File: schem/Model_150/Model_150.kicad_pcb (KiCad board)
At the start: 2 copper layers, 300 x 200 mm, 321 parts, among them SW1 RESET, SW2 POWER, U0 74LS00, U1 74LS04, U10 MAX232, U11 MAX232, U12 74LS00, U13 74HCT74, U14 74LS32, U15 74LS02, U16 74LS161, U17 74LS00, U18 74AHCT125, U19 74LS04, U2 DS1233, U20 74HCT138, U21 74LS74, U22 74LS139, U23 74LS32, U24 74HCT273, U25 DS1302+, U26 74AHCT125, U27 82C55A, U28 74LS04, U29 74HCT138, U3 74AHCT125, U30 74LS08, U33 4049UB, U34 74LS76, U35 74LS76, U37 LM555xN, U38 4070, U39 74LS161, U4 74HCT139, U40 74LS00, U41 74LS161, U42 74LS74, U43 4046, U5 74HCT688, U6 74HCT273, U7 74HCT157, U8 74HCT138, U9 74HCT273

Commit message: update model 150 files to Kicad 10 (from Kicad 9)
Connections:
- D6 pad 1: Net-(D6-K) -> -12V
- D6 pad 2: -12V -> Net-(D6-A)
- D8 pad 1: Net-(D8-K) -> -5V
- D8 pad 2: -5V -> Net-(D8-A)
- R12 pad 2: Net-(D6-K) -> Net-(D6-A)
- R14 pad 2: Net-(D8-K) -> Net-(D8-A)

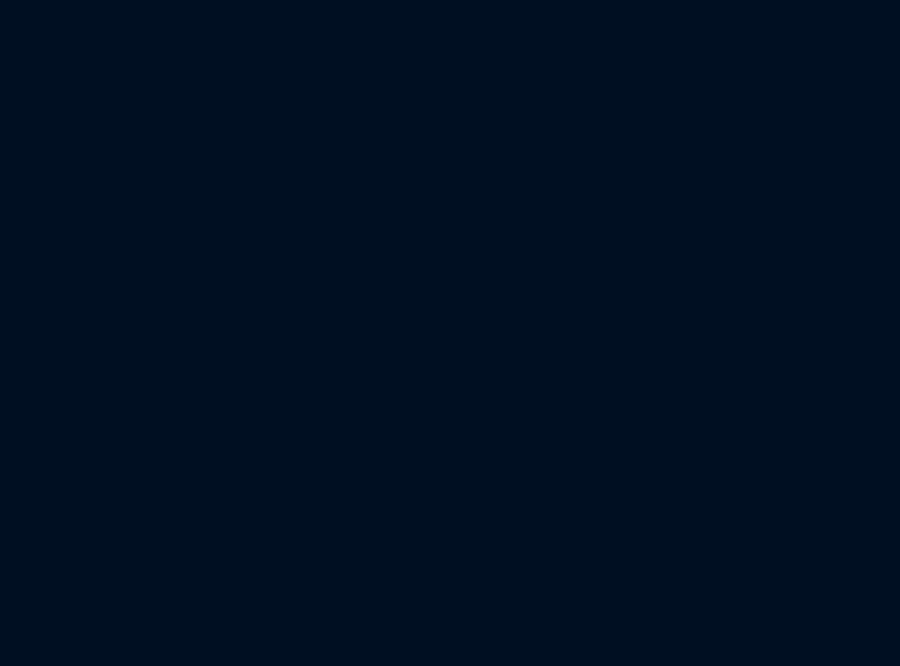
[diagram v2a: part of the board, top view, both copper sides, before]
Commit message: Assign nets, add JP5 header, add backups
Add numerous Model_150 backup ZIPs and update KiCad project files. Model_150.kicad_pcb: replace many "unconnected-..." net placeholders with proper net names (A0..A31, D0..D15, A#/D# mappings for ROM/JCBUS/IDE/FDD signals), fix a sheet path UUID, and update some testpoint/net assignments. Also add a new footprint: Connector_PinHeader_2.54mm:PinHeader_1x03 (JP5) with properties for RAM_SELECT. Project/schematic/report files were updated to reflect these changes.
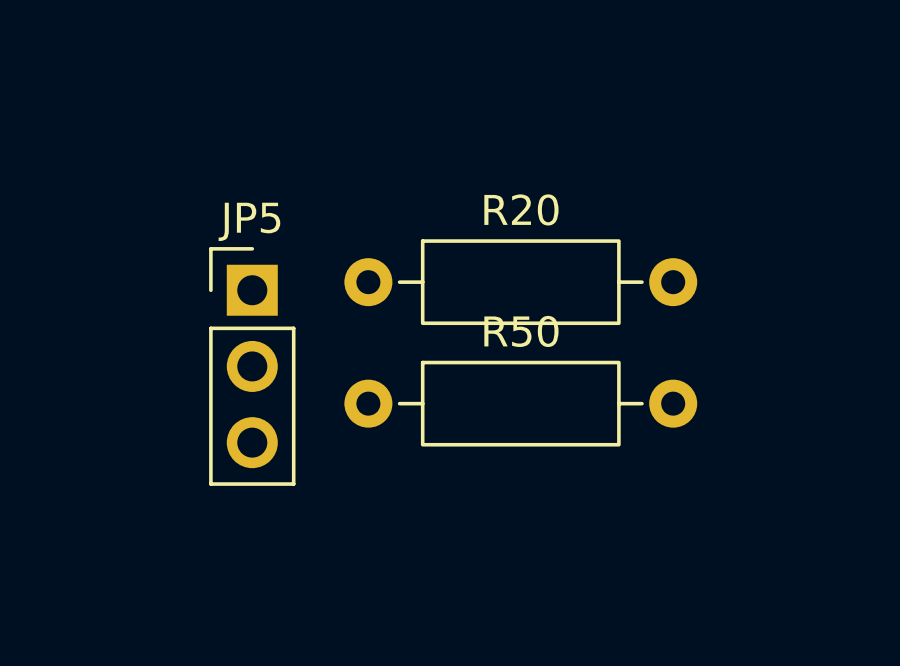
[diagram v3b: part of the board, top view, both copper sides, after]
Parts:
- added JP5: RAM_SELECT, Connector_PinHeader_2.54mm:PinHeader_1x03_P2.54mm_Vertical, F.Cu at (189.6, 45.1)
- added R20: 100K, Resistor_THT:R_Axial_DIN0207_L6.3mm_D2.5mm_P10.16mm_Horizontal, F.Cu at (193.5, 44.8)
- added R50: 100K, Resistor_THT:R_Axial_DIN0207_L6.3mm_D2.5mm_P10.16mm_Horizontal, F.Cu at (193.5, 48.9)
- R7: value R -> R?
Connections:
- net Net-(FDC_0-TC) renamed /TC
- net Net-(FDC_0-~{DACK}) renamed /DACK
- net Net-(U27-PA7) renamed /PA7
- net Net-(U4A-A0) renamed /MA19
- net Net-(U4B-A0) renamed /LA19
- net Net-(U6-Q1) renamed /LA15
- net Net-(U6-Q2) renamed /LA16
- net Net-(U6-Q3) renamed /LA17
- net Net-(U6-Q4) renamed /LA18
- CPU_0 pad 1: unconnected-(CPU_0-A11-Pad1) -> A11
- CPU_0 pad 10: unconnected-(CPU_0-D6-Pad10) -> D6
- CPU_0 pad 12: unconnected-(CPU_0-D2-Pad12) -> D2
- CPU_0 pad 13: unconnected-(CPU_0-D7-Pad13) -> D7
- CPU_0 pad 14: unconnected-(CPU_0-D0-Pad14) -> D0
- CPU_0 pad 15: unconnected-(CPU_0-D1-Pad15) -> D1
- CPU_0 pad 2: unconnected-(CPU_0-A12-Pad2) -> A12
- CPU_0 pad 3: unconnected-(CPU_0-A13-Pad3) -> A13
- CPU_0 pad 30: unconnected-(CPU_0-A0-Pad30) -> A0
- CPU_0 pad 31: unconnected-(CPU_0-A1-Pad31) -> A1
- CPU_0 pad 32: unconnected-(CPU_0-A2-Pad32) -> A2
- CPU_0 pad 33: unconnected-(CPU_0-A3-Pad33) -> A3
- CPU_0 pad 34: unconnected-(CPU_0-A4-Pad34) -> A4
- CPU_0 pad 35: unconnected-(CPU_0-A5-Pad35) -> A5
- CPU_0 pad 36: unconnected-(CPU_0-A6-Pad36) -> A6
- CPU_0 pad 37: unconnected-(CPU_0-A7-Pad37) -> A7
- CPU_0 pad 38: unconnected-(CPU_0-A8-Pad38) -> A8
- CPU_0 pad 39: unconnected-(CPU_0-A9-Pad39) -> A9
- CPU_0 pad 4: unconnected-(CPU_0-A14-Pad4) -> A14
- CPU_0 pad 40: unconnected-(CPU_0-A10-Pad40) -> A10
- CPU_0 pad 5: unconnected-(CPU_0-A15-Pad5) -> A15
- CPU_0 pad 7: unconnected-(CPU_0-D4-Pad7) -> D4
- CPU_0 pad 8: unconnected-(CPU_0-D3-Pad8) -> D3
- CPU_0 pad 9: unconnected-(CPU_0-D5-Pad9) -> D5
- CTC_0 pad 1: unconnected-(CTC_0-D4-Pad1) -> D4
- CTC_0 pad 18: unconnected-(CTC_0-CS0-Pad18) -> A0
- CTC_0 pad 19: unconnected-(CTC_0-CS1-Pad19) -> A1
- CTC_0 pad 2: unconnected-(CTC_0-D5-Pad2) -> D5
- CTC_0 pad 25: unconnected-(CTC_0-D0-Pad25) -> D0
- CTC_0 pad 26: unconnected-(CTC_0-D1-Pad26) -> D1
- CTC_0 pad 27: unconnected-(CTC_0-D2-Pad27) -> D2
- CTC_0 pad 28: unconnected-(CTC_0-D3-Pad28) -> D3
- CTC_0 pad 3: unconnected-(CTC_0-D6-Pad3) -> D6
- CTC_0 pad 4: unconnected-(CTC_0-D7-Pad4) -> D7
- DMA_0 pad 1: unconnected-(DMA_0-A5-Pad1) -> A5
- DMA_0 pad 17: unconnected-(DMA_0-A15-Pad17) -> A15
- DMA_0 pad 18: unconnected-(DMA_0-A14-Pad18) -> A14
- DMA_0 pad 19: unconnected-(DMA_0-A13-Pad19) -> A13
- DMA_0 pad 2: unconnected-(DMA_0-A4-Pad2) -> A4
- DMA_0 pad 20: unconnected-(DMA_0-A12-Pad20) -> A12
- DMA_0 pad 21: unconnected-(DMA_0-A11-Pad21) -> A11
- DMA_0 pad 22: unconnected-(DMA_0-A10-Pad22) -> A10
- DMA_0 pad 23: unconnected-(DMA_0-A9-Pad23) -> A9
- DMA_0 pad 24: unconnected-(DMA_0-A8-Pad24) -> A8
- DMA_0 pad 27: unconnected-(DMA_0-D7-Pad27) -> D7
- DMA_0 pad 28: unconnected-(DMA_0-D6-Pad28) -> D6
- DMA_0 pad 29: unconnected-(DMA_0-D5-Pad29) -> D5
- DMA_0 pad 3: unconnected-(DMA_0-A3-Pad3) -> A3
- DMA_0 pad 31: unconnected-(DMA_0-D4-Pad31) -> D4
- DMA_0 pad 32: unconnected-(DMA_0-D3-Pad32) -> D3
- DMA_0 pad 33: unconnected-(DMA_0-D2-Pad33) -> D2
- DMA_0 pad 34: unconnected-(DMA_0-D1-Pad34) -> D1
- DMA_0 pad 35: unconnected-(DMA_0-D0-Pad35) -> D0
- DMA_0 pad 39: unconnected-(DMA_0-A7-Pad39) -> A7
- DMA_0 pad 4: unconnected-(DMA_0-A2-Pad4) -> A2
- DMA_0 pad 40: unconnected-(DMA_0-A6-Pad40) -> A6
- DMA_0 pad 5: unconnected-(DMA_0-A1-Pad5) -> A1
- DMA_0 pad 6: unconnected-(DMA_0-A0-Pad6) -> A0
- FDC_0 pad 10: unconnected-(FDC_0-DB3-Pad10) -> D3
- FDC_0 pad 11: unconnected-(FDC_0-DB4-Pad11) -> D4
- FDC_0 pad 12: unconnected-(FDC_0-DB5-Pad12) -> D5
- FDC_0 pad 13: unconnected-(FDC_0-DB6-Pad13) -> D6
- FDC_0 pad 14: unconnected-(FDC_0-DB7-Pad14) -> D7
- FDC_0 pad 4: ADDRESS -> A[0..31]
- FDC_0 pad 7: unconnected-(FDC_0-DB0-Pad7) -> D0
- FDC_0 pad 8: unconnected-(FDC_0-DB1-Pad8) -> D1
- FDC_0 pad 9: unconnected-(FDC_0-DB2-Pad9) -> D2
- FDD_0 pad 34: Net-(FDC_0-WP) -> Net-(FDD_0-Pin_34)
- FPU_0 pad 10: unconnected-(FPU_0-DB2-Pad10) -> D2
- FPU_0 pad 11: unconnected-(FPU_0-DB3-Pad11) -> D3
- FPU_0 pad 12: unconnected-(FPU_0-DB4-Pad12) -> D4
- FPU_0 pad 13: unconnected-(FPU_0-DB5-Pad13) -> D5
- FPU_0 pad 14: unconnected-(FPU_0-DB6-Pad14) -> D6
- FPU_0 pad 15: unconnected-(FPU_0-DB7-Pad15) -> D7
- FPU_0 pad 21: ADDRESS -> A[0..31]
- FPU_0 pad 8: unconnected-(FPU_0-DB0-Pad8) -> D0
- FPU_0 pad 9: unconnected-(FPU_0-DB1-Pad9) -> D1
- IDE_1 pad 33: unconnected-(IDE_1-Pin_33-Pad33) -> A1
- IDE_1 pad 35: unconnected-(IDE_1-Pin_35-Pad35) -> A0
- IDE_1 pad 36: unconnected-(IDE_1-Pin_36-Pad36) -> A2
- JCBUS_0 pad a10: unconnected-(JCBUS_0-Pin_a10-Pada10) -> A1
- JCBUS_0 pad a11: unconnected-(JCBUS_0-Pin_a11-Pada11) -> A2
- JCBUS_0 pad a12: unconnected-(JCBUS_0-Pin_a12-Pada12) -> A3
- JCBUS_0 pad a13: unconnected-(JCBUS_0-Pin_a13-Pada13) -> A4
- JCBUS_0 pad a14: unconnected-(JCBUS_0-Pin_a14-Pada14) -> A5
- JCBUS_0 pad a15: unconnected-(JCBUS_0-Pin_a15-Pada15) -> A6
- JCBUS_0 pad a16: unconnected-(JCBUS_0-Pin_a16-Pada16) -> A7
- JCBUS_0 pad a17: unconnected-(JCBUS_0-Pin_a17-Pada17) -> A8
- JCBUS_0 pad a18: unconnected-(JCBUS_0-Pin_a18-Pada18) -> A9
- JCBUS_0 pad a19: unconnected-(JCBUS_0-Pin_a19-Pada19) -> A10
- JCBUS_0 pad a20: unconnected-(JCBUS_0-Pin_a20-Pada20) -> A11
- JCBUS_0 pad a21: unconnected-(JCBUS_0-Pin_a21-Pada21) -> A12
- JCBUS_0 pad a22: unconnected-(JCBUS_0-Pin_a22-Pada22) -> A13
- JCBUS_0 pad a23: unconnected-(JCBUS_0-Pin_a23-Pada23) -> A14
- JCBUS_0 pad a24: unconnected-(JCBUS_0-Pin_a24-Pada24) -> A15
- JCBUS_0 pad a25: unconnected-(JCBUS_0-Pin_a25-Pada25) -> A16
- JCBUS_0 pad a26: unconnected-(JCBUS_0-Pin_a26-Pada26) -> A17
- JCBUS_0 pad a27: unconnected-(JCBUS_0-Pin_a27-Pada27) -> A18
- JCBUS_0 pad a28: unconnected-(JCBUS_0-Pin_a28-Pada28) -> A19
- JCBUS_0 pad a29: unconnected-(JCBUS_0-Pin_a29-Pada29) -> A20
- JCBUS_0 pad a30: unconnected-(JCBUS_0-Pin_a30-Pada30) -> A21
- JCBUS_0 pad a31: unconnected-(JCBUS_0-Pin_a31-Pada31) -> A22
- JCBUS_0 pad a32: unconnected-(JCBUS_0-Pin_a32-Pada32) -> A23
- JCBUS_0 pad a33: unconnected-(JCBUS_0-Pin_a33-Pada33) -> A24
- JCBUS_0 pad a34: unconnected-(JCBUS_0-Pin_a34-Pada34) -> A25
- JCBUS_0 pad a35: unconnected-(JCBUS_0-Pin_a35-Pada35) -> A26
- JCBUS_0 pad a36: unconnected-(JCBUS_0-Pin_a36-Pada36) -> A27
- JCBUS_0 pad a37: unconnected-(JCBUS_0-Pin_a37-Pada37) -> A28
- JCBUS_0 pad a38: unconnected-(JCBUS_0-Pin_a38-Pada38) -> A29
- JCBUS_0 pad a39: unconnected-(JCBUS_0-Pin_a39-Pada39) -> A30
- JCBUS_0 pad a40: unconnected-(JCBUS_0-Pin_a40-Pada40) -> A31
- JCBUS_0 pad a9: unconnected-(JCBUS_0-Pin_a9-Pada9) -> A0
- JCBUS_0 pad b25: unconnected-(JCBUS_0-Pin_b25-Padb25) -> D0
- JCBUS_0 pad b26: unconnected-(JCBUS_0-Pin_b26-Padb26) -> D1
- JCBUS_0 pad b27: unconnected-(JCBUS_0-Pin_b27-Padb27) -> D2
- JCBUS_0 pad b28: unconnected-(JCBUS_0-Pin_b28-Padb28) -> D3
- JCBUS_0 pad b29: unconnected-(JCBUS_0-Pin_b29-Padb29) -> D4
- JCBUS_0 pad b30: unconnected-(JCBUS_0-Pin_b30-Padb30) -> D5
- JCBUS_0 pad b31: unconnected-(JCBUS_0-Pin_b31-Padb31) -> D6
- JCBUS_0 pad b32: unconnected-(JCBUS_0-Pin_b32-Padb32) -> D7
- JCBUS_0 pad b33: unconnected-(JCBUS_0-Pin_b33-Padb33) -> D8
- JCBUS_0 pad b34: unconnected-(JCBUS_0-Pin_b34-Padb34) -> D9
- JCBUS_0 pad b35: unconnected-(JCBUS_0-Pin_b35-Padb35) -> D10
- JCBUS_0 pad b36: unconnected-(JCBUS_0-Pin_b36-Padb36) -> D11
- JCBUS_0 pad b37: unconnected-(JCBUS_0-Pin_b37-Padb37) -> D12
- JCBUS_0 pad b38: unconnected-(JCBUS_0-Pin_b38-Padb38) -> D13
- JCBUS_0 pad b39: unconnected-(JCBUS_0-Pin_b39-Padb39) -> D14
- JCBUS_0 pad b40: unconnected-(JCBUS_0-Pin_b40-Padb40) -> D15
- JCBUS_1 pad a10: unconnected-(JCBUS_1-Pin_a10-Pada10) -> A1
- JCBUS_1 pad a11: unconnected-(JCBUS_1-Pin_a11-Pada11) -> A2
- JCBUS_1 pad a12: unconnected-(JCBUS_1-Pin_a12-Pada12) -> A3
- JCBUS_1 pad a13: unconnected-(JCBUS_1-Pin_a13-Pada13) -> A4
- JCBUS_1 pad a14: unconnected-(JCBUS_1-Pin_a14-Pada14) -> A5
- JCBUS_1 pad a15: unconnected-(JCBUS_1-Pin_a15-Pada15) -> A6
- JCBUS_1 pad a16: unconnected-(JCBUS_1-Pin_a16-Pada16) -> A7
- JCBUS_1 pad a17: unconnected-(JCBUS_1-Pin_a17-Pada17) -> A8
- JCBUS_1 pad a18: unconnected-(JCBUS_1-Pin_a18-Pada18) -> A9
- JCBUS_1 pad a19: unconnected-(JCBUS_1-Pin_a19-Pada19) -> A10
- JCBUS_1 pad a20: unconnected-(JCBUS_1-Pin_a20-Pada20) -> A11
- JCBUS_1 pad a21: unconnected-(JCBUS_1-Pin_a21-Pada21) -> A12
- JCBUS_1 pad a22: unconnected-(JCBUS_1-Pin_a22-Pada22) -> A13
- JCBUS_1 pad a23: unconnected-(JCBUS_1-Pin_a23-Pada23) -> A14
- JCBUS_1 pad a24: unconnected-(JCBUS_1-Pin_a24-Pada24) -> A15
- JCBUS_1 pad a25: unconnected-(JCBUS_1-Pin_a25-Pada25) -> A16
- JCBUS_1 pad a26: unconnected-(JCBUS_1-Pin_a26-Pada26) -> A17
- JCBUS_1 pad a27: unconnected-(JCBUS_1-Pin_a27-Pada27) -> A18
- JCBUS_1 pad a28: unconnected-(JCBUS_1-Pin_a28-Pada28) -> A19
- JCBUS_1 pad a29: unconnected-(JCBUS_1-Pin_a29-Pada29) -> A20
- JCBUS_1 pad a30: unconnected-(JCBUS_1-Pin_a30-Pada30) -> A21
- JCBUS_1 pad a31: unconnected-(JCBUS_1-Pin_a31-Pada31) -> A22
- JCBUS_1 pad a32: unconnected-(JCBUS_1-Pin_a32-Pada32) -> A23
- JCBUS_1 pad a33: unconnected-(JCBUS_1-Pin_a33-Pada33) -> A24
- JCBUS_1 pad a34: unconnected-(JCBUS_1-Pin_a34-Pada34) -> A25
- JCBUS_1 pad a35: unconnected-(JCBUS_1-Pin_a35-Pada35) -> A26
- JCBUS_1 pad a36: unconnected-(JCBUS_1-Pin_a36-Pada36) -> A27
- JCBUS_1 pad a37: unconnected-(JCBUS_1-Pin_a37-Pada37) -> A28
- JCBUS_1 pad a38: unconnected-(JCBUS_1-Pin_a38-Pada38) -> A29
- JCBUS_1 pad a39: unconnected-(JCBUS_1-Pin_a39-Pada39) -> A30
- JCBUS_1 pad a40: unconnected-(JCBUS_1-Pin_a40-Pada40) -> A31
- JCBUS_1 pad a9: unconnected-(JCBUS_1-Pin_a9-Pada9) -> A0
- JCBUS_1 pad b25: unconnected-(JCBUS_1-Pin_b25-Padb25) -> D0
- JCBUS_1 pad b26: unconnected-(JCBUS_1-Pin_b26-Padb26) -> D1
- JCBUS_1 pad b27: unconnected-(JCBUS_1-Pin_b27-Padb27) -> D2
- JCBUS_1 pad b28: unconnected-(JCBUS_1-Pin_b28-Padb28) -> D3
- JCBUS_1 pad b29: unconnected-(JCBUS_1-Pin_b29-Padb29) -> D4
- JCBUS_1 pad b30: unconnected-(JCBUS_1-Pin_b30-Padb30) -> D5
- JCBUS_1 pad b31: unconnected-(JCBUS_1-Pin_b31-Padb31) -> D6
- JCBUS_1 pad b32: unconnected-(JCBUS_1-Pin_b32-Padb32) -> D7
- JCBUS_1 pad b33: unconnected-(JCBUS_1-Pin_b33-Padb33) -> D8
- JCBUS_1 pad b34: unconnected-(JCBUS_1-Pin_b34-Padb34) -> D9
- JCBUS_1 pad b35: unconnected-(JCBUS_1-Pin_b35-Padb35) -> D10
- JCBUS_1 pad b36: unconnected-(JCBUS_1-Pin_b36-Padb36) -> D11
- JCBUS_1 pad b37: unconnected-(JCBUS_1-Pin_b37-Padb37) -> D12
- JCBUS_1 pad b38: unconnected-(JCBUS_1-Pin_b38-Padb38) -> D13
- JCBUS_1 pad b39: unconnected-(JCBUS_1-Pin_b39-Padb39) -> D14
- JCBUS_1 pad b40: unconnected-(JCBUS_1-Pin_b40-Padb40) -> D15
- JCBUS_2 pad a10: unconnected-(JCBUS_2-Pin_a10-Pada10) -> A1
- JCBUS_2 pad a11: unconnected-(JCBUS_2-Pin_a11-Pada11) -> A2
- JCBUS_2 pad a12: unconnected-(JCBUS_2-Pin_a12-Pada12) -> A3
- JCBUS_2 pad a13: unconnected-(JCBUS_2-Pin_a13-Pada13) -> A4
- JCBUS_2 pad a14: unconnected-(JCBUS_2-Pin_a14-Pada14) -> A5
- JCBUS_2 pad a15: unconnected-(JCBUS_2-Pin_a15-Pada15) -> A6
- JCBUS_2 pad a16: unconnected-(JCBUS_2-Pin_a16-Pada16) -> A7
- JCBUS_2 pad a17: unconnected-(JCBUS_2-Pin_a17-Pada17) -> A8
- JCBUS_2 pad a18: unconnected-(JCBUS_2-Pin_a18-Pada18) -> A9
- JCBUS_2 pad a19: unconnected-(JCBUS_2-Pin_a19-Pada19) -> A10
- JCBUS_2 pad a20: unconnected-(JCBUS_2-Pin_a20-Pada20) -> A11
- JCBUS_2 pad a21: unconnected-(JCBUS_2-Pin_a21-Pada21) -> A12
- JCBUS_2 pad a22: unconnected-(JCBUS_2-Pin_a22-Pada22) -> A13
- JCBUS_2 pad a23: unconnected-(JCBUS_2-Pin_a23-Pada23) -> A14
- JCBUS_2 pad a24: unconnected-(JCBUS_2-Pin_a24-Pada24) -> A15
- JCBUS_2 pad a25: unconnected-(JCBUS_2-Pin_a25-Pada25) -> A16
- JCBUS_2 pad a26: unconnected-(JCBUS_2-Pin_a26-Pada26) -> A17
- JCBUS_2 pad a27: unconnected-(JCBUS_2-Pin_a27-Pada27) -> A18
- JCBUS_2 pad a28: unconnected-(JCBUS_2-Pin_a28-Pada28) -> A19
- JCBUS_2 pad a29: unconnected-(JCBUS_2-Pin_a29-Pada29) -> A20
- JCBUS_2 pad a30: unconnected-(JCBUS_2-Pin_a30-Pada30) -> A21
- JCBUS_2 pad a31: unconnected-(JCBUS_2-Pin_a31-Pada31) -> A22
- JCBUS_2 pad a32: unconnected-(JCBUS_2-Pin_a32-Pada32) -> A23
- JCBUS_2 pad a33: unconnected-(JCBUS_2-Pin_a33-Pada33) -> A24
- JCBUS_2 pad a34: unconnected-(JCBUS_2-Pin_a34-Pada34) -> A25
- JCBUS_2 pad a35: unconnected-(JCBUS_2-Pin_a35-Pada35) -> A26
- JCBUS_2 pad a36: unconnected-(JCBUS_2-Pin_a36-Pada36) -> A27
- JCBUS_2 pad a37: unconnected-(JCBUS_2-Pin_a37-Pada37) -> A28
- JCBUS_2 pad a38: unconnected-(JCBUS_2-Pin_a38-Pada38) -> A29
- JCBUS_2 pad a39: unconnected-(JCBUS_2-Pin_a39-Pada39) -> A30
- JCBUS_2 pad a40: unconnected-(JCBUS_2-Pin_a40-Pada40) -> A31
- JCBUS_2 pad a9: unconnected-(JCBUS_2-Pin_a9-Pada9) -> A0
- JCBUS_2 pad b25: unconnected-(JCBUS_2-Pin_b25-Padb25) -> D0
- JCBUS_2 pad b26: unconnected-(JCBUS_2-Pin_b26-Padb26) -> D1
- JCBUS_2 pad b27: unconnected-(JCBUS_2-Pin_b27-Padb27) -> D2
- JCBUS_2 pad b28: unconnected-(JCBUS_2-Pin_b28-Padb28) -> D3
- JCBUS_2 pad b29: unconnected-(JCBUS_2-Pin_b29-Padb29) -> D4
- JCBUS_2 pad b30: unconnected-(JCBUS_2-Pin_b30-Padb30) -> D5
- JCBUS_2 pad b31: unconnected-(JCBUS_2-Pin_b31-Padb31) -> D6
- JCBUS_2 pad b32: unconnected-(JCBUS_2-Pin_b32-Padb32) -> D7
- JCBUS_2 pad b33: unconnected-(JCBUS_2-Pin_b33-Padb33) -> D8
- JCBUS_2 pad b34: unconnected-(JCBUS_2-Pin_b34-Padb34) -> D9
- JCBUS_2 pad b35: unconnected-(JCBUS_2-Pin_b35-Padb35) -> D10
- JCBUS_2 pad b36: unconnected-(JCBUS_2-Pin_b36-Padb36) -> D11
- JCBUS_2 pad b37: unconnected-(JCBUS_2-Pin_b37-Padb37) -> D12
- JCBUS_2 pad b38: unconnected-(JCBUS_2-Pin_b38-Padb38) -> D13
- JCBUS_2 pad b39: unconnected-(JCBUS_2-Pin_b39-Padb39) -> D14
- JCBUS_2 pad b40: unconnected-(JCBUS_2-Pin_b40-Padb40) -> D15
- JCBUS_3 pad a10: unconnected-(JCBUS_3-Pin_a10-Pada10) -> A1
- JCBUS_3 pad a11: unconnected-(JCBUS_3-Pin_a11-Pada11) -> A2
- JCBUS_3 pad a12: unconnected-(JCBUS_3-Pin_a12-Pada12) -> A3
- JCBUS_3 pad a13: unconnected-(JCBUS_3-Pin_a13-Pada13) -> A4
- JCBUS_3 pad a14: unconnected-(JCBUS_3-Pin_a14-Pada14) -> A5
- JCBUS_3 pad a15: unconnected-(JCBUS_3-Pin_a15-Pada15) -> A6
- JCBUS_3 pad a16: unconnected-(JCBUS_3-Pin_a16-Pada16) -> A7
- JCBUS_3 pad a17: unconnected-(JCBUS_3-Pin_a17-Pada17) -> A8
- JCBUS_3 pad a18: unconnected-(JCBUS_3-Pin_a18-Pada18) -> A9
- JCBUS_3 pad a19: unconnected-(JCBUS_3-Pin_a19-Pada19) -> A10
- JCBUS_3 pad a20: unconnected-(JCBUS_3-Pin_a20-Pada20) -> A11
- JCBUS_3 pad a21: unconnected-(JCBUS_3-Pin_a21-Pada21) -> A12
- JCBUS_3 pad a22: unconnected-(JCBUS_3-Pin_a22-Pada22) -> A13
- JCBUS_3 pad a23: unconnected-(JCBUS_3-Pin_a23-Pada23) -> A14
- JCBUS_3 pad a24: unconnected-(JCBUS_3-Pin_a24-Pada24) -> A15
- JCBUS_3 pad a25: unconnected-(JCBUS_3-Pin_a25-Pada25) -> A16
- JCBUS_3 pad a26: unconnected-(JCBUS_3-Pin_a26-Pada26) -> A17
- JCBUS_3 pad a27: unconnected-(JCBUS_3-Pin_a27-Pada27) -> A18
- JCBUS_3 pad a28: unconnected-(JCBUS_3-Pin_a28-Pada28) -> A19
- JCBUS_3 pad a29: unconnected-(JCBUS_3-Pin_a29-Pada29) -> A20
- JCBUS_3 pad a30: unconnected-(JCBUS_3-Pin_a30-Pada30) -> A21
- JCBUS_3 pad a31: unconnected-(JCBUS_3-Pin_a31-Pada31) -> A22
- JCBUS_3 pad a32: unconnected-(JCBUS_3-Pin_a32-Pada32) -> A23
- JCBUS_3 pad a33: unconnected-(JCBUS_3-Pin_a33-Pada33) -> A24
- JCBUS_3 pad a34: unconnected-(JCBUS_3-Pin_a34-Pada34) -> A25
- JCBUS_3 pad a35: unconnected-(JCBUS_3-Pin_a35-Pada35) -> A26
- JCBUS_3 pad a36: unconnected-(JCBUS_3-Pin_a36-Pada36) -> A27
- JCBUS_3 pad a37: unconnected-(JCBUS_3-Pin_a37-Pada37) -> A28
- JCBUS_3 pad a38: unconnected-(JCBUS_3-Pin_a38-Pada38) -> A29
- JCBUS_3 pad a39: unconnected-(JCBUS_3-Pin_a39-Pada39) -> A30
- JCBUS_3 pad a40: unconnected-(JCBUS_3-Pin_a40-Pada40) -> A31
- JCBUS_3 pad a9: unconnected-(JCBUS_3-Pin_a9-Pada9) -> A0
- JCBUS_3 pad b25: unconnected-(JCBUS_3-Pin_b25-Padb25) -> D0
- JCBUS_3 pad b26: unconnected-(JCBUS_3-Pin_b26-Padb26) -> D1
- JCBUS_3 pad b27: unconnected-(JCBUS_3-Pin_b27-Padb27) -> D2
- JCBUS_3 pad b28: unconnected-(JCBUS_3-Pin_b28-Padb28) -> D3
- JCBUS_3 pad b29: unconnected-(JCBUS_3-Pin_b29-Padb29) -> D4
- JCBUS_3 pad b30: unconnected-(JCBUS_3-Pin_b30-Padb30) -> D5
- JCBUS_3 pad b31: unconnected-(JCBUS_3-Pin_b31-Padb31) -> D6
- JCBUS_3 pad b32: unconnected-(JCBUS_3-Pin_b32-Padb32) -> D7
- JCBUS_3 pad b33: unconnected-(JCBUS_3-Pin_b33-Padb33) -> D8
- JCBUS_3 pad b34: unconnected-(JCBUS_3-Pin_b34-Padb34) -> D9
- JCBUS_3 pad b35: unconnected-(JCBUS_3-Pin_b35-Padb35) -> D10
- JCBUS_3 pad b36: unconnected-(JCBUS_3-Pin_b36-Padb36) -> D11
- JCBUS_3 pad b37: unconnected-(JCBUS_3-Pin_b37-Padb37) -> D12
- JCBUS_3 pad b38: unconnected-(JCBUS_3-Pin_b38-Padb38) -> D13
- JCBUS_3 pad b39: unconnected-(JCBUS_3-Pin_b39-Padb39) -> D14
- JCBUS_3 pad b40: unconnected-(JCBUS_3-Pin_b40-Padb40) -> D15
- JCBUS_4 pad a10: unconnected-(JCBUS_4-Pin_a10-Pada10) -> A1
- JCBUS_4 pad a11: unconnected-(JCBUS_4-Pin_a11-Pada11) -> A2
- JCBUS_4 pad a12: unconnected-(JCBUS_4-Pin_a12-Pada12) -> A3
- JCBUS_4 pad a13: unconnected-(JCBUS_4-Pin_a13-Pada13) -> A4
- JCBUS_4 pad a14: unconnected-(JCBUS_4-Pin_a14-Pada14) -> A5
- JCBUS_4 pad a15: unconnected-(JCBUS_4-Pin_a15-Pada15) -> A6
- JCBUS_4 pad a16: unconnected-(JCBUS_4-Pin_a16-Pada16) -> A7
- JCBUS_4 pad a17: unconnected-(JCBUS_4-Pin_a17-Pada17) -> A8
- JCBUS_4 pad a18: unconnected-(JCBUS_4-Pin_a18-Pada18) -> A9
- JCBUS_4 pad a19: unconnected-(JCBUS_4-Pin_a19-Pada19) -> A10
- JCBUS_4 pad a20: unconnected-(JCBUS_4-Pin_a20-Pada20) -> A11
- JCBUS_4 pad a21: unconnected-(JCBUS_4-Pin_a21-Pada21) -> A12
- JCBUS_4 pad a22: unconnected-(JCBUS_4-Pin_a22-Pada22) -> A13
- JCBUS_4 pad a23: unconnected-(JCBUS_4-Pin_a23-Pada23) -> A14
- JCBUS_4 pad a24: unconnected-(JCBUS_4-Pin_a24-Pada24) -> A15
- JCBUS_4 pad a25: unconnected-(JCBUS_4-Pin_a25-Pada25) -> A16
- JCBUS_4 pad a26: unconnected-(JCBUS_4-Pin_a26-Pada26) -> A17
- JCBUS_4 pad a27: unconnected-(JCBUS_4-Pin_a27-Pada27) -> A18
- JCBUS_4 pad a28: unconnected-(JCBUS_4-Pin_a28-Pada28) -> A19
- JCBUS_4 pad a29: unconnected-(JCBUS_4-Pin_a29-Pada29) -> A20
- JCBUS_4 pad a30: unconnected-(JCBUS_4-Pin_a30-Pada30) -> A21
- JCBUS_4 pad a31: unconnected-(JCBUS_4-Pin_a31-Pada31) -> A22
- JCBUS_4 pad a32: unconnected-(JCBUS_4-Pin_a32-Pada32) -> A23
- JCBUS_4 pad a33: unconnected-(JCBUS_4-Pin_a33-Pada33) -> A24
- JCBUS_4 pad a34: unconnected-(JCBUS_4-Pin_a34-Pada34) -> A25
- JCBUS_4 pad a35: unconnected-(JCBUS_4-Pin_a35-Pada35) -> A26
- JCBUS_4 pad a36: unconnected-(JCBUS_4-Pin_a36-Pada36) -> A27
- JCBUS_4 pad a37: unconnected-(JCBUS_4-Pin_a37-Pada37) -> A28
- JCBUS_4 pad a38: unconnected-(JCBUS_4-Pin_a38-Pada38) -> A29
- JCBUS_4 pad a39: unconnected-(JCBUS_4-Pin_a39-Pada39) -> A30
- JCBUS_4 pad a40: unconnected-(JCBUS_4-Pin_a40-Pada40) -> A31
- JCBUS_4 pad a9: unconnected-(JCBUS_4-Pin_a9-Pada9) -> A0
- JCBUS_4 pad b25: unconnected-(JCBUS_4-Pin_b25-Padb25) -> D0
- JCBUS_4 pad b26: unconnected-(JCBUS_4-Pin_b26-Padb26) -> D1
- JCBUS_4 pad b27: unconnected-(JCBUS_4-Pin_b27-Padb27) -> D2
- JCBUS_4 pad b28: unconnected-(JCBUS_4-Pin_b28-Padb28) -> D3
- JCBUS_4 pad b29: unconnected-(JCBUS_4-Pin_b29-Padb29) -> D4
- JCBUS_4 pad b30: unconnected-(JCBUS_4-Pin_b30-Padb30) -> D5
- JCBUS_4 pad b31: unconnected-(JCBUS_4-Pin_b31-Padb31) -> D6
- JCBUS_4 pad b32: unconnected-(JCBUS_4-Pin_b32-Padb32) -> D7
- JCBUS_4 pad b33: unconnected-(JCBUS_4-Pin_b33-Padb33) -> D8
- JCBUS_4 pad b34: unconnected-(JCBUS_4-Pin_b34-Padb34) -> D9
- JCBUS_4 pad b35: unconnected-(JCBUS_4-Pin_b35-Padb35) -> D10
- JCBUS_4 pad b36: unconnected-(JCBUS_4-Pin_b36-Padb36) -> D11
- JCBUS_4 pad b37: unconnected-(JCBUS_4-Pin_b37-Padb37) -> D12
- JCBUS_4 pad b38: unconnected-(JCBUS_4-Pin_b38-Padb38) -> D13
- JCBUS_4 pad b39: unconnected-(JCBUS_4-Pin_b39-Padb39) -> D14
- JCBUS_4 pad b40: unconnected-(JCBUS_4-Pin_b40-Padb40) -> D15
- JCBUS_5 pad a10: unconnected-(JCBUS_5-Pin_a10-Pada10) -> A1
- JCBUS_5 pad a11: unconnected-(JCBUS_5-Pin_a11-Pada11) -> A2
- JCBUS_5 pad a12: unconnected-(JCBUS_5-Pin_a12-Pada12) -> A3
- JCBUS_5 pad a13: unconnected-(JCBUS_5-Pin_a13-Pada13) -> A4
- JCBUS_5 pad a14: unconnected-(JCBUS_5-Pin_a14-Pada14) -> A5
- JCBUS_5 pad a15: unconnected-(JCBUS_5-Pin_a15-Pada15) -> A6
- JCBUS_5 pad a16: unconnected-(JCBUS_5-Pin_a16-Pada16) -> A7
- JCBUS_5 pad a17: unconnected-(JCBUS_5-Pin_a17-Pada17) -> A8
- JCBUS_5 pad a18: unconnected-(JCBUS_5-Pin_a18-Pada18) -> A9
- JCBUS_5 pad a19: unconnected-(JCBUS_5-Pin_a19-Pada19) -> A10
- JCBUS_5 pad a20: unconnected-(JCBUS_5-Pin_a20-Pada20) -> A11
- JCBUS_5 pad a21: unconnected-(JCBUS_5-Pin_a21-Pada21) -> A12
- JCBUS_5 pad a22: unconnected-(JCBUS_5-Pin_a22-Pada22) -> A13
- JCBUS_5 pad a23: unconnected-(JCBUS_5-Pin_a23-Pada23) -> A14
- JCBUS_5 pad a24: unconnected-(JCBUS_5-Pin_a24-Pada24) -> A15
- JCBUS_5 pad a25: unconnected-(JCBUS_5-Pin_a25-Pada25) -> A16
- JCBUS_5 pad a26: unconnected-(JCBUS_5-Pin_a26-Pada26) -> A17
- JCBUS_5 pad a27: unconnected-(JCBUS_5-Pin_a27-Pada27) -> A18
- JCBUS_5 pad a28: unconnected-(JCBUS_5-Pin_a28-Pada28) -> A19
- JCBUS_5 pad a29: unconnected-(JCBUS_5-Pin_a29-Pada29) -> A20
- JCBUS_5 pad a30: unconnected-(JCBUS_5-Pin_a30-Pada30) -> A21
- JCBUS_5 pad a31: unconnected-(JCBUS_5-Pin_a31-Pada31) -> A22
- JCBUS_5 pad a32: unconnected-(JCBUS_5-Pin_a32-Pada32) -> A23
- JCBUS_5 pad a33: unconnected-(JCBUS_5-Pin_a33-Pada33) -> A24
- JCBUS_5 pad a34: unconnected-(JCBUS_5-Pin_a34-Pada34) -> A25
- JCBUS_5 pad a35: unconnected-(JCBUS_5-Pin_a35-Pada35) -> A26
- JCBUS_5 pad a36: unconnected-(JCBUS_5-Pin_a36-Pada36) -> A27
- JCBUS_5 pad a37: unconnected-(JCBUS_5-Pin_a37-Pada37) -> A28
- JCBUS_5 pad a38: unconnected-(JCBUS_5-Pin_a38-Pada38) -> A29
- JCBUS_5 pad a39: unconnected-(JCBUS_5-Pin_a39-Pada39) -> A30
- JCBUS_5 pad a40: unconnected-(JCBUS_5-Pin_a40-Pada40) -> A31
- JCBUS_5 pad a9: unconnected-(JCBUS_5-Pin_a9-Pada9) -> A0
- JCBUS_5 pad b25: unconnected-(JCBUS_5-Pin_b25-Padb25) -> D0
- JCBUS_5 pad b26: unconnected-(JCBUS_5-Pin_b26-Padb26) -> D1
- JCBUS_5 pad b27: unconnected-(JCBUS_5-Pin_b27-Padb27) -> D2
- JCBUS_5 pad b28: unconnected-(JCBUS_5-Pin_b28-Padb28) -> D3
- JCBUS_5 pad b29: unconnected-(JCBUS_5-Pin_b29-Padb29) -> D4
- JCBUS_5 pad b30: unconnected-(JCBUS_5-Pin_b30-Padb30) -> D5
- JCBUS_5 pad b31: unconnected-(JCBUS_5-Pin_b31-Padb31) -> D6
- JCBUS_5 pad b32: unconnected-(JCBUS_5-Pin_b32-Padb32) -> D7
- JCBUS_5 pad b33: unconnected-(JCBUS_5-Pin_b33-Padb33) -> D8
- JCBUS_5 pad b34: unconnected-(JCBUS_5-Pin_b34-Padb34) -> D9
- JCBUS_5 pad b35: unconnected-(JCBUS_5-Pin_b35-Padb35) -> D10
- JCBUS_5 pad b36: unconnected-(JCBUS_5-Pin_b36-Padb36) -> D11
- JCBUS_5 pad b37: unconnected-(JCBUS_5-Pin_b37-Padb37) -> D12
- JCBUS_5 pad b38: unconnected-(JCBUS_5-Pin_b38-Padb38) -> D13
- JCBUS_5 pad b39: unconnected-(JCBUS_5-Pin_b39-Padb39) -> D14
- JCBUS_5 pad b40: unconnected-(JCBUS_5-Pin_b40-Padb40) -> D15
- PIO_0 pad 1: unconnected-(PIO_0-D2-Pad1) -> D2
- PIO_0 pad 19: unconnected-(PIO_0-D0-Pad19) -> D0
- PIO_0 pad 2: unconnected-(PIO_0-D7-Pad2) -> D7
- PIO_0 pad 20: unconnected-(PIO_0-D1-Pad20) -> D1
- PIO_0 pad 3: unconnected-(PIO_0-D6-Pad3) -> D6
- PIO_0 pad 38: unconnected-(PIO_0-D5-Pad38) -> D5
- PIO_0 pad 39: unconnected-(PIO_0-D4-Pad39) -> D4
- PIO_0 pad 40: unconnected-(PIO_0-D3-Pad40) -> D3
- PIO_0 pad 5: unconnected-(PIO_0-C/~{D}-Pad5) -> A1
- PIO_0 pad 6: unconnected-(PIO_0-B/~{A}-Pad6) -> A0
- R19 pad 2: Net-(JP5-A) -> Net-(JP5-B)
- RAM_0 pad 10: unconnected-(RAM_0-A2-Pad10) -> A2
- RAM_0 pad 11: unconnected-(RAM_0-A1-Pad11) -> A1
- RAM_0 pad 12: unconnected-(RAM_0-A0-Pad12) -> A0
- RAM_0 pad 13: unconnected-(RAM_0-DQ0-Pad13) -> D0
- RAM_0 pad 14: unconnected-(RAM_0-DQ1-Pad14) -> D1
- RAM_0 pad 15: unconnected-(RAM_0-DQ2-Pad15) -> D2
- RAM_0 pad 17: unconnected-(RAM_0-DQ3-Pad17) -> D3
- RAM_0 pad 18: unconnected-(RAM_0-DQ4-Pad18) -> D4
- RAM_0 pad 19: unconnected-(RAM_0-DQ5-Pad19) -> D5
- RAM_0 pad 20: unconnected-(RAM_0-DQ6-Pad20) -> D6
- RAM_0 pad 21: unconnected-(RAM_0-DQ7-Pad21) -> D7
- RAM_0 pad 22: Net-(JP5-A) -> Net-(JP5-B)
- RAM_0 pad 23: unconnected-(RAM_0-A10-Pad23) -> A10
- RAM_0 pad 25: unconnected-(RAM_0-A11-Pad25) -> A11
- RAM_0 pad 26: unconnected-(RAM_0-A9-Pad26) -> A9
- RAM_0 pad 27: unconnected-(RAM_0-A8-Pad27) -> A8
- RAM_0 pad 28: unconnected-(RAM_0-A13-Pad28) -> A13
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
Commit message: Add docs and update Model_150 schematics/backups
Add two storage PDFs to docs/storage. Reorganize Model_150 backups: delete outdated zips, rename many timestamped backup archives, and add several new backup zip files. Update KiCad project files (Model_150.kicad_pcb, .kicad_pro, .kicad_sch), update the Carboni_Library symbol file and its backup, and refresh report.txt. PCB changes include adding a board stackup, adjusting footprints (positions/rotations), setting pad orientations, and updating UUIDs and fabrication parameters to keep the project consistent for manufacture and tracking.
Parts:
- removed the JP5 at (189.6, 45.1)
- removed the R20 at (193.5, 44.8)
- removed the R50 at (193.5, 48.9)
- added JP1: XOSC_CLK, Connector_PinHeader_2.54mm:PinHeader_1x02_P2.54mm_Vertical, F.Cu at (137.3, 239.8)
- added JP2: XRES_CLK2, Connector_PinHeader_2.54mm:PinHeader_1x02_P2.54mm_Vertical, F.Cu at (146.3, 239.8)
- added JP34: DMA_FDC, Connector_PinHeader_2.54mm:PinHeader_1x02_P2.54mm_Vertical, F.Cu at (253.8, 86.0)
- added TP1: GND, TestPoint:TestPoint_THTPad_1.5x1.5mm_Drill0.7mm, F.Cu at (44.5, 68.6)
- added TP1: GND, TestPoint:TestPoint_THTPad_1.5x1.5mm_Drill0.7mm, F.Cu at (44.5, 66.0)
- added TP1: GND, TestPoint:TestPoint_THTPad_1.5x1.5mm_Drill0.7mm, F.Cu at (44.5, 63.5)
- added TP1: GND, TestPoint:TestPoint_THTPad_1.5x1.5mm_Drill0.7mm, F.Cu at (44.5, 193.0)
- added TP1: GND, TestPoint:TestPoint_THTPad_1.5x1.5mm_Drill0.7mm, F.Cu at (44.5, 61.0)
- added TP1: GND, TestPoint:TestPoint_THTPad_1.5x1.5mm_Drill0.7mm, F.Cu at (44.5, 190.5)
- added TP10: CLK2, TestPoint:TestPoint_THTPad_1.5x1.5mm_Drill0.7mm, F.Cu at (154.3, 244.0)
- added TP121: NC, TestPoint:TestPoint_THTPad_1.5x1.5mm_Drill0.7mm, F.Cu at (41.9, 180.3)
- added TP122: NC, TestPoint:TestPoint_THTPad_1.5x1.5mm_Drill0.7mm, F.Cu at (41.9, 182.9)
- added TP123: NC, TestPoint:TestPoint_THTPad_1.5x1.5mm_Drill0.7mm, F.Cu at (41.9, 185.4)
- added TP124: NC, TestPoint:TestPoint_THTPad_1.5x1.5mm_Drill0.7mm, F.Cu at (41.9, 188.0)
- added TP125: RESET, TestPoint:TestPoint_THTPad_1.5x1.5mm_Drill0.7mm, F.Cu at (41.9, 73.7)
- added TP2: +5V, TestPoint:TestPoint_THTPad_1.5x1.5mm_Drill0.7mm, F.Cu at (41.9, 190.5)
- added TP2: +5V, TestPoint:TestPoint_THTPad_1.5x1.5mm_Drill0.7mm, F.Cu at (41.9, 61.0)
- added TP22: BUSREQ, TestPoint:TestPoint_THTPad_1.5x1.5mm_Drill0.7mm, F.Cu at (41.9, 104.1)
- added TP23: BUSAK, TestPoint:TestPoint_THTPad_1.5x1.5mm_Drill0.7mm, F.Cu at (41.9, 106.7)
- added TP3: +12V, TestPoint:TestPoint_THTPad_1.5x1.5mm_Drill0.7mm, F.Cu at (41.9, 63.5)
- added TP3: +12V, TestPoint:TestPoint_THTPad_1.5x1.5mm_Drill0.7mm, F.Cu at (41.9, 193.0)
- added TP5: -12V, TestPoint:TestPoint_THTPad_1.5x1.5mm_Drill0.7mm, F.Cu at (41.9, 66.0)
- added TP6: +3.3V, TestPoint:TestPoint_THTPad_1.5x1.5mm_Drill0.7mm, F.Cu at (41.9, 68.6)
- added TP9: CLK, TestPoint:TestPoint_THTPad_1.5x1.5mm_Drill0.7mm, F.Cu at (154.3, 249.0)
- FPU_0: footprint Package_DIP:DIP-24_W15.24mm_Socket -> Package_DIP:DIP-24_W15.24mm
- R10, R11, R12, R13, R14, R8, R9: value R -> R220
- R7: value R? -> R220
- TP23: value BUSAK -> BUSACK
- moved TP24 229.1 mm to (250.2, 96.1)
- moved TP23 224.8 mm to (245.4, 69.8)
- moved TP22 224.8 mm to (244.1, 63.5)
- moved TP10 193.5 mm to (41.9, 71.1)
- moved TP9 186.3 mm to (41.9, 76.2)
- moved U26 84.8 mm to (183.4, 256.7)
- moved U24 82.0 mm to (166.9, 253.1)
- moved JP32 76.9 mm to (246.0, 85.8)
- moved JP31 76.9 mm to (241.4, 85.8)
- moved TP60 65.4 mm to (44.5, 106.7)
- moved TP59 64.5 mm to (44.5, 104.1)
- moved TP58 63.6 mm to (44.5, 101.6)
- moved TP57 62.7 mm to (44.5, 99.1)
- moved TP56 61.8 mm to (44.5, 96.5)
- moved TP55 60.9 mm to (44.5, 94.0)
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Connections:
- C22 pad 1: Net-(C22-Pad1) -> +5V
- C22 pad 2: Net-(C22-Pad2) -> GND
- CPU_0 pad 23: BUSAK -> BUSACK
- CPU_0 pad 25: BUSRQ -> BUSREQ
- FDC_0 pad 15: unconnected-(FDC_0-DMA-Pad15) -> Net-(FDC_0-DMA)
- FDC_0 pad 4: A[0..31] -> A0
- FPU_0 pad 21: A[0..31] -> A0
- FPU_0 pad 6: (no net) -> unconnected-(FPU_0-NC-Pad6)
- FPU_0 pad 7: (no net) -> unconnected-(FPU_0-NC-Pad7)
- IDE_0 pad 10: unconnected-(IDE_0-Pin_10-Pad10) -> /PB3
- IDE_0 pad 11: unconnected-(IDE_0-Pin_11-Pad11) -> /PA3
- IDE_0 pad 12: unconnected-(IDE_0-Pin_12-Pad12) -> /PB4
- IDE_0 pad 13: unconnected-(IDE_0-Pin_13-Pad13) -> /PA2
- IDE_0 pad 14: unconnected-(IDE_0-Pin_14-Pad14) -> /PB5
- IDE_0 pad 15: unconnected-(IDE_0-Pin_15-Pad15) -> /PA1
- IDE_0 pad 16: unconnected-(IDE_0-Pin_16-Pad16) -> /PB6
- IDE_0 pad 17: unconnected-(IDE_0-Pin_17-Pad17) -> /PA0
- IDE_0 pad 18: unconnected-(IDE_0-Pin_18-Pad18) -> /PB7
- IDE_0 pad 3: unconnected-(IDE_0-Pin_3-Pad3) -> /PA7
- IDE_0 pad 4: unconnected-(IDE_0-Pin_4-Pad4) -> /PB0
- IDE_0 pad 5: unconnected-(IDE_0-Pin_5-Pad5) -> /PA6
- IDE_0 pad 6: unconnected-(IDE_0-Pin_6-Pad6) -> /PB1
- IDE_0 pad 7: unconnected-(IDE_0-Pin_7-Pad7) -> /PA5
- IDE_0 pad 8: unconnected-(IDE_0-Pin_8-Pad8) -> /PB2
- IDE_0 pad 9: unconnected-(IDE_0-Pin_9-Pad9) -> /PA4
- JCBUS_5 pad b45: unconnected-(JCBUS_5-Pin_b45-Padb45) -> Net-(JCBUS_5-Pin_b45)
- JCBUS_5 pad b46: unconnected-(JCBUS_5-Pin_b46-Padb46) -> Net-(JCBUS_5-Pin_b46)
- JCBUS_5 pad b47: unconnected-(JCBUS_5-Pin_b47-Padb47) -> Net-(JCBUS_5-Pin_b47)
- JCBUS_5 pad b48: unconnected-(JCBUS_5-Pin_b48-Padb48) -> Net-(JCBUS_5-Pin_b48)
- R3 pad 2: BUSRQ -> BUSREQ
- SIO_0 pad 33: Net-(SIO_0-C/~{D}) -> Net-(JP33-C)
- TP120 pad 1: Net-(U34B-J) -> Net-(U34A-Q)
- TP23 pad 1: BUSAK -> BUSACK
- U0 pad 14: GND -> +5VSB
- U0 pad 7: +5VSB -> GND
- U1 pad 8: Net-(SIO_0-C/~{D}) -> Net-(JP33-B)
- U27 pad 8: unconnected-(U27-A1-Pad8) -> A1
- U27 pad 9: unconnected-(U27-A0-Pad9) -> A0
- U30 pad 11: unconnected-(U30-Pad11) -> Net-(IDE_1-Pin_37)
- U30 pad 12: unconnected-(U30-Pad12) -> M1
- U30 pad 13: unconnected-(U30-Pad13) -> Net-(U15-Pad1)
- U33 pad 2: Net-(U35A-J) -> Net-(U34A-J)
- U34 pad 1: (no net) -> Net-(U16-Q3)
- U34 pad 12: Net-(U34B-J) -> Net-(U34A-Q)
- U34 pad 14: (no net) -> unconnected-(U34A-~{Q}-Pad14)
- U34 pad 15: (no net) -> Net-(U34A-Q)
- U34 pad 16: (no net) -> Net-(U34A-J)
- U34 pad 2: (no net) -> Net-(JP40-B)
- U34 pad 3: (no net) -> +5V
- U34 pad 4: (no net) -> Net-(U34A-J)
- U34 pad 9: Net-(U34B-J) -> Net-(U34A-Q)
- XTAL_OSC_0 pad 4: +5V -> GND
- XTAL_OSC_0 pad 5: (no net) -> Net-(JP1-A)
- XTAL_OSC_0 pad 8: (no net) -> +5V
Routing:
- net +5V: track 0.00 -> 484.7 mm
- net +12V: track 0.00 -> 484.7 mm
- net DACK1: track 0.00 -> 138.0 mm
- net A10: track 0.00 -> 138.0 mm
- net TX2: track 0.00 -> 138.0 mm
- net DREQ2: track 0.00 -> 138.0 mm
- net DREQ0: track 0.00 -> 138.0 mm
- net DACK3: track 0.00 -> 138.0 mm
- net DACK0: track 0.00 -> 138.0 mm
- net A3: track 0.00 -> 138.0 mm
- net A29: track 0.00 -> 138.0 mm
- net A28: track 0.00 -> 138.0 mm
- net A25: track 0.00 -> 138.0 mm
- net A24: track 0.00 -> 138.0 mm
- net A21: track 0.00 -> 138.0 mm
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
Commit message: Update Model_150 PCB and tidy backups
Bump PCB revision and apply footprint/layout fixes. Updated Model_150.kicad_pcb (rev 1→2): replaced THT capacitor footprint to 2.00mm pin pitch, adjusted reference/value positions and silkscreen lines, and regenerated UUIDs/effects. Updated project/schematic files and symbol libraries (Carboni and Zilog). Added PDF exports and updated report.txt. Also cleaned up, renamed and added many files under schem/Model_150/Model_150-backups (removed old backups, added new ones, and renamed several archives).
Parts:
- removed U35: 74LS76, Package_DIP:DIP-16_W7.62mm
- added ?: , , F.Cu at (164.8, 63.5)
- added ?: , , F.Cu at (162.3, 68.6)
- added ?: , , F.Cu at (164.8, 61.0)
- added ?: , , F.Cu at (162.3, 63.5)
- added ?: , , F.Cu at (162.3, 190.5)
- added ?: , , F.Cu at (164.8, 193.0)
- added ?: , , F.Cu at (164.8, 68.6)
- added ?: , , F.Cu at (162.3, 66.0)
- added ?: , , F.Cu at (164.8, 66.0)
- added ?: , , F.Cu at (164.8, 190.5)
- added ?: , , F.Cu at (162.3, 193.0)
- added ?: , , F.Cu at (162.3, 61.0)
- added C15: 100nF, Capacitor_THT:C_Disc_D5.0mm_W2.5mm_P2.50mm, F.Cu at (75.9, 266.2)
- added C18: 100nF, Capacitor_THT:C_Disc_D5.0mm_W2.5mm_P2.50mm, F.Cu at (75.9, 270.2)
- added C19: 100nF, Capacitor_THT:C_Disc_D5.0mm_W2.5mm_P2.50mm, F.Cu at (82.5, 254.0)
- added C20: 100nF, Capacitor_THT:C_Disc_D5.0mm_W2.5mm_P2.50mm, F.Cu at (82.5, 258.1)
- added C21: 100nF, Capacitor_THT:C_Disc_D5.0mm_W2.5mm_P2.50mm, F.Cu at (82.5, 262.1)
- added C23: 100nF, Capacitor_THT:C_Disc_D5.0mm_W2.5mm_P2.50mm, F.Cu at (82.5, 266.2)
- added C26: 100nF, Capacitor_THT:C_Disc_D5.0mm_W2.5mm_P2.50mm, F.Cu at (82.5, 270.2)
- added C29: 100nF, Capacitor_THT:C_Disc_D5.0mm_W2.5mm_P2.50mm, F.Cu at (89.0, 254.0)
- added C30: 100nF, Capacitor_THT:C_Disc_D5.0mm_W2.5mm_P2.50mm, F.Cu at (89.0, 258.1)
- added C31: 22nF, Capacitor_THT:C_Rect_L7.0mm_W3.5mm_P5.00mm, F.Cu at (270.2, 204.3)
- added C34: 2.1uF, Capacitor_THT:C_Radial_D5.0mm_H11.0mm_P2.00mm, F.Cu at (264.1, 205.1)
- added C35: 100pF, Capacitor_THT:C_Disc_D3.4mm_W2.1mm_P2.50mm, F.Cu at (270.0, 208.7)
- added C36: 100pF, Capacitor_THT:C_Disc_D3.4mm_W2.1mm_P2.50mm, F.Cu at (270.0, 212.3)
- added C37: 2.2uF, Capacitor_THT:C_Radial_D5.0mm_H11.0mm_P2.00mm, F.Cu at (264.1, 211.6)
- added C38: 100nF, Capacitor_THT:C_Disc_D5.0mm_W2.5mm_P2.50mm, F.Cu at (89.0, 262.1)
- added C39: 100nF, Capacitor_THT:C_Disc_D5.0mm_W2.5mm_P2.50mm, F.Cu at (89.0, 266.2)
- added C4: 100nF, Capacitor_THT:C_Disc_D5.0mm_W2.5mm_P2.50mm, F.Cu at (75.9, 254.0)
- added C40: 100nF, Capacitor_THT:C_Disc_D5.0mm_W2.5mm_P2.50mm, F.Cu at (89.0, 270.2)
- added C41: 100nF, Capacitor_THT:C_Disc_D5.0mm_W2.5mm_P2.50mm, F.Cu at (95.6, 254.0)
- added C42: 100nF, Capacitor_THT:C_Disc_D5.0mm_W2.5mm_P2.50mm, F.Cu at (95.6, 258.1)
- added C43: 100nF, Capacitor_THT:C_Disc_D5.0mm_W2.5mm_P2.50mm, F.Cu at (95.6, 262.1)
- added C44: 100nF, Capacitor_THT:C_Disc_D5.0mm_W2.5mm_P2.50mm, F.Cu at (95.6, 266.2)
- added C45: 100nF, Capacitor_THT:C_Disc_D5.0mm_W2.5mm_P2.50mm, F.Cu at (95.6, 270.2)
- added C5: 100nF, Capacitor_THT:C_Disc_D5.0mm_W2.5mm_P2.50mm, F.Cu at (75.9, 258.1)
- added C6: 100nF, Capacitor_THT:C_Disc_D5.0mm_W2.5mm_P2.50mm, F.Cu at (75.9, 262.1)
- added JP44: RST_RST2, Connector_PinHeader_2.54mm:PinHeader_1x02_P2.54mm_Vertical, F.Cu at (72.6, 217.3)
- added TP126: DMA_BAI, TestPoint:TestPoint_THTPad_1.5x1.5mm_Drill0.7mm, F.Cu at (281.6, 106.3)
- added TP127: BMA_BAO, TestPoint:TestPoint_THTPad_1.5x1.5mm_Drill0.7mm, F.Cu at (281.6, 109.9)
- added TP128: FDC_HDL, TestPoint:TestPoint_THTPad_1.5x1.5mm_Drill0.7mm, F.Cu at (395.1, 185.3)
- added TP129: FPU_SVACK, TestPoint:TestPoint_THTPad_1.5x1.5mm_Drill0.7mm, F.Cu at (281.1, 141.5)
- added TP130: FPU_SVREQ, TestPoint:TestPoint_THTPad_1.5x1.5mm_Drill0.7mm, F.Cu at (281.1, 145.0)
- C1, C24, C27: footprint Capacitor_THT:C_Disc_D3.0mm_W1.6mm_P2.50mm -> Capacitor_THT:C_Disc_D3.4mm_W2.1mm_P2.50mm
- C10, C11, C12, C13, C14, C7, C8, C9: footprint Capacitor_THT:CP_Radial_D4.0mm_P1.50mm -> Capacitor_THT:CP_Radial_D4.0mm_P2.00mm
- C16, C17, C2, C22, C25, C28, C3: footprint Capacitor_THT:C_Disc_D3.0mm_W1.6mm_P2.50mm -> Capacitor_THT:C_Disc_D5.0mm_W2.5mm_P2.50mm
- CTC_0: footprint Package_DIP:DIP-28_W15.24mm_Socket -> Package_DIP:DIP-28_W15.24mm_LongPads
- TP22: value BUSRQ -> BUSREQ
- TP23: value BUSAK -> BUSACK
- moved U17 286.1 mm to (205.8, 257.3)
- moved TP22 9.72 mm to (245.2, 73.2)
- moved TP23 5.84 mm to (245.2, 75.7)
- moved ATX_PWR_0 1.56 mm to (179.4, 198.2)
- moved TP114 1.29 mm to (275.9, 248.6)
- moved TP116 1.29 mm to (275.9, 255.7)
- moved TP117 1.29 mm to (275.9, 259.3)
- moved U37 1.29 mm to (272.1, 266.4)
- moved U43 1.29 mm to (283.5, 248.6)
- moved TP115 1.29 mm to (275.9, 252.2)
- moved U39 1.29 mm to (272.0, 223.9)
- moved U42 1.29 mm to (263.8, 245.8)
- moved R61 1.29 mm to (228.9, 249.8)
- moved R62 1.29 mm to (228.9, 253.9)
- moved R63 1.29 mm to (228.9, 257.9)
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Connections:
- DMA_0 pad 14: unconnected-(DMA_0-~{BAI}-Pad14) -> BUSACK
- JCBUS_5 pad b45: Net-(JCBUS_5-Pin_b45) -> unconnected-(JCBUS_5-Pin_b45-Padb45)
- JCBUS_5 pad b46: Net-(JCBUS_5-Pin_b46) -> unconnected-(JCBUS_5-Pin_b46-Padb46)
- JCBUS_5 pad b47: Net-(JCBUS_5-Pin_b47) -> unconnected-(JCBUS_5-Pin_b47-Padb47)
- JCBUS_5 pad b48: Net-(JCBUS_5-Pin_b48) -> unconnected-(JCBUS_5-Pin_b48-Padb48)
- TP121 pad 1: Net-(JCBUS_5-Pin_b45) -> unconnected-(JCBUS_5-Pin_b45-Padb45)
- TP122 pad 1: Net-(JCBUS_5-Pin_b46) -> unconnected-(JCBUS_5-Pin_b46-Padb46)
- TP123 pad 1: Net-(JCBUS_5-Pin_b47) -> unconnected-(JCBUS_5-Pin_b47-Padb47)
- TP124 pad 1: Net-(JCBUS_5-Pin_b48) -> unconnected-(JCBUS_5-Pin_b48-Padb48)
- TP22 pad 1: BUSRQ -> BUSREQ
- TP23 pad 1: BUSAK -> BUSACK
- U17 pad 10: M1 -> unconnected-(U17-Pad10)
- U17 pad 8: Net-(IDE_1-Pin_37) -> unconnected-(U17-Pad8)
- U17 pad 9: Net-(U15-Pad1) -> unconnected-(U17-Pad9)
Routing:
- net GND: track 116.8 -> 565.4 mm
- net BUSAK: track 135.4 -> 0.00 mm
- net BUSACK: track 0.00 -> 135.4 mm
- net (no net): track 0.00 -> 37.4 mm
- net +5V: track 484.7 -> 506.6 mm
- net +12V: track 484.7 -> 506.6 mm
- net -12V: track 116.7 -> 127.6 mm
- net +3.3V: track 116.7 -> 127.6 mm
- net Net-(JCBUS_5-Pin_b47): track 9.36 -> 0.00 mm
- net Net-(JCBUS_5-Pin_b46): track 9.36 -> 0.00 mm
- net Net-(JCBUS_5-Pin_b48): track 9.36 -> 0.00 mm
- net Net-(JCBUS_5-Pin_b45): track 9.36 -> 0.00 mm
